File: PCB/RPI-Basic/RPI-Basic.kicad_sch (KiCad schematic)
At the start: 2 parts, among them J1 SE2-30, J2 Conn_02x20_Odd_Even

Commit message: layed out board
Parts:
- added J3: Conn_02x20_Odd_Even, Connector_PinHeader_2.54mm:PinHeader_2x20_P2.54mm_Vertical, symbol Connector_Generic:Conn_02x20_Odd_Even
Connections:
- net +5V: now also J3.2 (Pin_2), J3.4 (Pin_4)
- net 0: now also J3.27 (Pin_27)
- net 1: now also J3.28 (Pin_28)
- net 10: now also J3.19 (Pin_19)
- net 11: now also J3.23 (Pin_23)
- net 12: now also J3.32 (Pin_32)
- net 13: now also J3.33 (Pin_33)
- net 14: now also J3.8 (Pin_8)
- net 15: now also J3.10 (Pin_10)
- net 16: now also J3.36 (Pin_36)
- net 17: now also J3.11 (Pin_11)
- net 18: now also J3.12 (Pin_12)
- net 19: now also J3.35 (Pin_35)
- net 2: now also J3.3 (Pin_3)
- net 20: now also J3.38 (Pin_38)
- net 21: now also J3.40 (Pin_40)
- net 22: now also J3.15 (Pin_15)
- net 23: now also J3.16 (Pin_16)
- net 24: now also J3.18 (Pin_18)
- net 25: now also J3.22 (Pin_22)
- net 26: now also J3.37 (Pin_37)
- net 27: now also J3.13 (Pin_13)
- net 3: now also J3.5 (Pin_5)
- net 4: now also J3.7 (Pin_7)
- net 5: now also J3.29 (Pin_29)
- net 6: now also J3.31 (Pin_31)
- net 7: now also J3.26 (Pin_26)
- net 8: now also J3.24 (Pin_24)
- net 9: now also J3.21 (Pin_21)
- net GND: now also J3.14 (Pin_14), J3.20 (Pin_20), J3.25 (Pin_25), J3.30 (Pin_30), J3.34 (Pin_34), J3.39 (Pin_39), J3.6 (Pin_6), J3.9 (Pin_9)
- removed net +3.3V: J1.23 (3.3V), J1.53 (3.3V), J2.1 (Pin_1), J2.17 (Pin_17)
- no-connect marks 4 -> 10

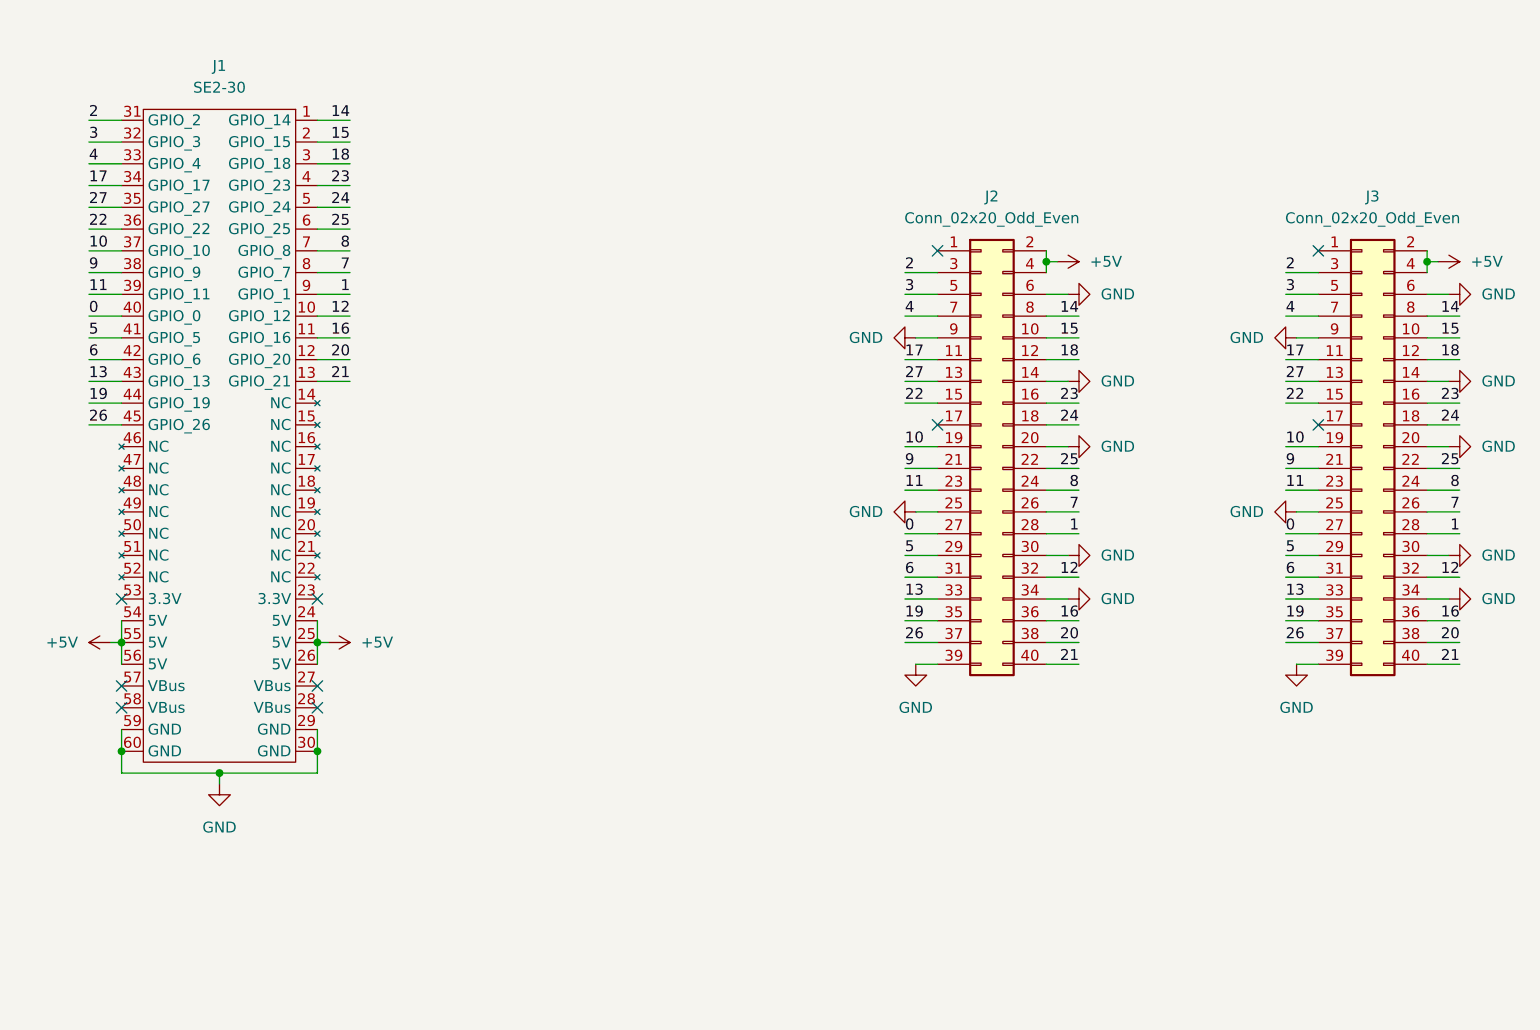
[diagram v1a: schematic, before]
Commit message: added support mounting
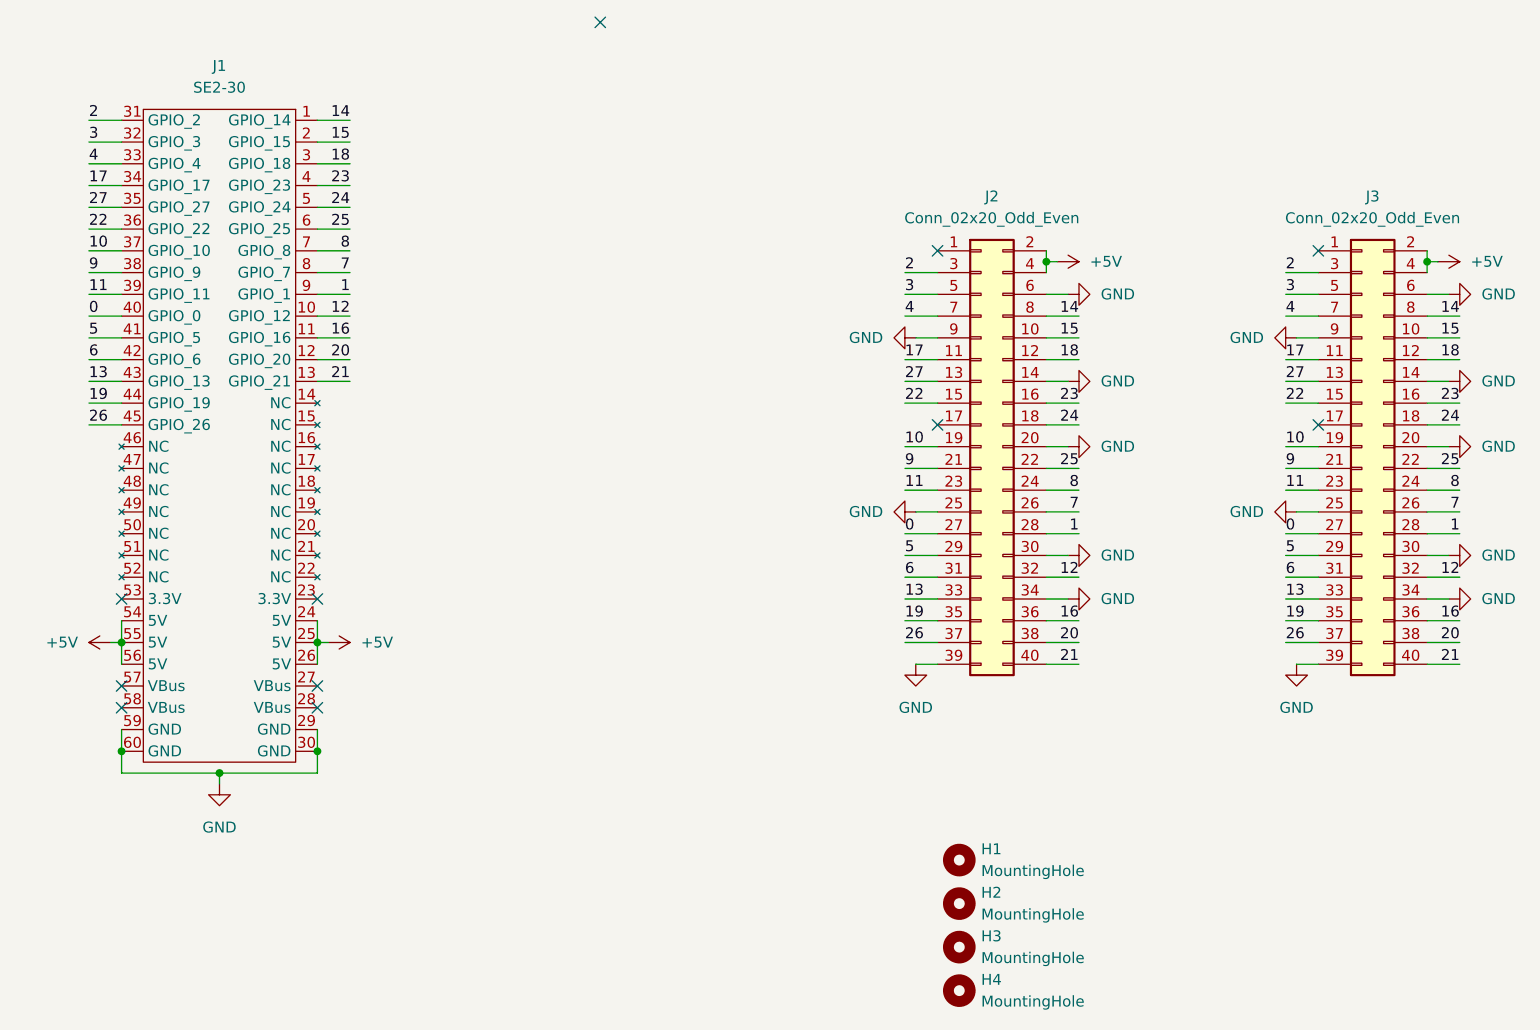
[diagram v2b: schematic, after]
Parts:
- added H1, H2, H3, H4: MountingHole, MountingHole:MountingHole_2.2mm_M2, symbol Mechanical:MountingHole
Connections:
- no-connect marks 10 -> 11
